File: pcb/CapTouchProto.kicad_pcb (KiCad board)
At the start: 2 copper layers, 12 parts, among them J1 62684-50110, U1 1965-ESP32-WROOM-32E(8MB)CT-ND

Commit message: A little layout.
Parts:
- added C4: 0.1μF, Capacitor_SMD:C_0603_1608Metric, F.Cu at (161.7, 155.1)
- added C5: 0.1μF, Capacitor_SMD:C_0603_1608Metric, F.Cu at (141.8, 126.2)
- added C6: 22μF, Capacitor_SMD:C_0603_1608Metric, F.Cu at (136.7, 123.8)
- added C7: 0.1μF, Capacitor_SMD:C_0603_1608Metric, F.Cu at (136.7, 125.5)
- added C8: 22μF, Capacitor_SMD:C_0603_1608Metric, F.Cu at (129.5, 134.0)
- added C9: 22μF, Capacitor_SMD:C_0603_1608Metric, F.Cu at (136.7, 127.9)
- added D1: BAT760-7, Diode_SMD:D_SOD-323, F.Cu at (108.8, 129.3)
- added D2: SP0503BAHT, Package_TO_SOT_SMD:SOT-143, F.Cu at (173.5, 135.8)
- added D3: LED (red), LED_SMD:LED_0603_1608Metric, F.Cu at (136.5, 138.7)
- added Q1: S8050, Package_TO_SOT_THT:TO-92_Inline, F.Cu at (163.7, 115.1)
- added Q2: S8050, Package_TO_SOT_THT:TO-92_Inline, F.Cu at (164.4, 111.2)
- added R10: 10K, Resistor_SMD:R_0603_1608Metric, F.Cu at (168.0, 113.1)
- added R11: 10KΩ, Resistor_SMD:R_0603_1608Metric, F.Cu at (140.0, 126.2)
- added R12: 2K (5%), Resistor_SMD:R_0603_1608Metric, F.Cu at (133.4, 138.7)
- added R13: 2K2Ω, Resistor_SMD:R_0603_1608Metric, F.Cu at (136.6, 98.1)
- added R14: 2K2Ω, Resistor_SMD:R_0603_1608Metric, F.Cu at (136.6, 96.3)
- added R15: 68Ω, Resistor_SMD:R_0603_1608Metric, F.Cu at (159.6, 92.1)
- added R16: 68Ω, Resistor_SMD:R_0603_1608Metric, F.Cu at (159.6, 93.9)
- added R17: 68Ω, Resistor_SMD:R_0603_1608Metric, F.Cu at (159.6, 95.8)
- added R18: 68Ω, Resistor_SMD:R_0603_1608Metric, F.Cu at (159.6, 97.6)
- added R8: 10KΩ, Resistor_SMD:R_0603_1608Metric, F.Cu at (132.0, 157.0)
- added R9: 10K, Resistor_SMD:R_0603_1608Metric, F.Cu at (160.2, 113.1)
- added SW1: SW_Push, Button_Switch_THT:SW_PUSH_6mm_H4.3mm, F.Cu at (148.1, 96.3)
- added SW2: SW_Push, Button_Switch_THT:SW_PUSH_6mm_H4.3mm, F.Cu at (159.3, 151.3)
- added U2: 1965-ESP32-WROOM-32E(8MB)CT-ND, RF_Module:ESP32-WROOM-32, F.Cu at (144.5, 113.0)
- added U3: AMS1117-3.3, Package_TO_SOT_SMD:SOT-223-3_TabPin2, F.Cu at (136.6, 132.7)
- C1: value 22μF -> 4.7μF/6.3V; footprint Capacitor_SMD:C_0201_0603Metric -> Capacitor_SMD:C_0603_1608Metric
- C2: value 0.1μF -> 0.1μF/50V; footprint Capacitor_SMD:C_0201_0603Metric -> Capacitor_SMD:C_0603_1608Metric
- C3: value TBD -> 0.1μF; footprint Capacitor_SMD:C_0201_0603Metric -> Capacitor_SMD:C_0603_1608Metric
- R1: value 2K2Ω -> 22.1KΩ; footprint Resistor_SMD:R_0201_0603Metric -> Resistor_SMD:R_0603_1608Metric
- R2: value 2K2Ω -> 47.5KΩ; footprint Resistor_SMD:R_0201_0603Metric -> Resistor_SMD:R_0603_1608Metric
- R3, R5: value 68Ω -> 5K1Ω; footprint Resistor_SMD:R_0201_0603Metric -> Resistor_SMD:R_0603_1608Metric
- R4: value 68Ω -> 2KΩ; footprint Resistor_SMD:R_0201_0603Metric -> Resistor_SMD:R_0603_1608Metric
- R6: value 68Ω -> 0Ω; footprint Resistor_SMD:R_0201_0603Metric -> Resistor_SMD:R_0603_1608Metric
- R7: value TBDΩ -> 0Ω; footprint Resistor_SMD:R_0201_0603Metric -> Resistor_SMD:R_0603_1608Metric
- U1: value 1965-ESP32-WROOM-32E(8MB)CT-ND -> CP2102N-A01-GQFN28; footprint RF_Module:ESP32-WROOM-32 -> Package_DFN_QFN:QFN-28-1EP_5x5mm_P0.5mm_EP3.35x3.35mm
- moved C2 84.3 mm to (115.7, 146.4), turned to 270 degrees
- moved R3 83.0 mm to (108.8, 138.4), turned to 180 degrees
- moved R2 74.6 mm to (135.3, 148.2)
- moved R1 70.1 mm to (145.9, 144.8)
- moved R4 68.3 mm to (136.7, 143.7), turned to 180 degrees
- moved U1 52.7 mm to (122.3, 144.1)
- moved R7 51.9 mm to (141.5, 101.3), turned to 90 degrees
- moved C1 40.1 mm to (117.5, 146.4), turned to 270 degrees
- moved R5 37.6 mm to (108.6, 134.1), turned to 180 degrees
- moved C3 35.6 mm to (150.2, 86.6)
- moved R6 31.1 mm to (139.8, 101.3), turned to 90 degrees
- moved J2 9.79 mm to (174.1, 85.9), turned to 90 degrees
- renumbered J1 to J2
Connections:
- C1 pad 1: +3V3 -> VBUS
- C2 pad 1: +3V3 -> VBUS
- C3 pad 1: Net-(C3-Pad1) -> GND
- C3 pad 2: GND -> IO0
- J2 pad 10: Net-(J1-Pad10) -> Net-(J2-Pad10)
- J2 pad 2: Net-(J1-Pad2) -> Net-(J2-Pad2)
- J2 pad 3: Net-(J1-Pad3) -> Net-(J2-Pad3)
- J2 pad 33: Net-(J1-Pad33) -> Net-(J2-Pad33)
- J2 pad 34: Net-(J1-Pad34) -> Net-(J2-Pad34)
- J2 pad 36: Net-(J1-Pad36) -> Net-(J2-Pad36)
- J2 pad 37: Net-(J1-Pad37) -> Net-(J2-Pad37)
- J2 pad 38: Net-(J1-Pad38) -> Net-(J2-Pad38)
- J2 pad 4: Net-(J1-Pad4) -> Net-(J2-Pad4)
- J2 pad 44: Net-(J1-Pad44) -> Net-(J2-Pad44)
- J2 pad 45: Net-(J1-Pad45) -> Net-(J2-Pad45)
- J2 pad 46: Net-(J1-Pad46) -> Net-(J2-Pad46)
- J2 pad 47: Net-(J1-Pad10) -> Net-(J2-Pad10)
- J2 pad 5: Net-(J1-Pad5) -> Net-(J2-Pad5)
- R1 pad 1: +3V3 -> VBUS
- R1 pad 2: Net-(J1-Pad44) -> Net-(R1-Pad2)
- R2 pad 1: +3V3 -> Net-(R1-Pad2)
- R2 pad 2: Net-(J1-Pad45) -> GND
- R3 pad 1: Net-(J1-Pad2) -> Net-(J1-PadA5)
- R3 pad 2: +5V -> GND
- R4 pad 1: Net-(J1-Pad3) -> +3V3
- R4 pad 2: +5V -> Net-(R4-Pad2)
- R5 pad 1: Net-(J1-Pad4) -> Net-(J1-PadA5)
- R5 pad 2: +5V -> Net-(R5-Pad2)
- R6 pad 1: Net-(J1-Pad5) -> TXD
- R6 pad 2: +5V -> Net-(R6-Pad2)
- R7 pad 1: +3V3 -> RXD
- R7 pad 2: Net-(C3-Pad1) -> Net-(R7-Pad2)
- U1 pad 1: GND -> Net-(U1-Pad1)
- U1 pad 10: Net-(J1-Pad46) -> Net-(U1-Pad10)
- U1 pad 11: Net-(J1-Pad36) -> Net-(R8-Pad1)
- U1 pad 12: Net-(J1-Pad10) -> Net-(U1-Pad12)
- U1 pad 15: GND -> Net-(U1-Pad15)
- U1 pad 2: +3V3 -> Net-(U1-Pad2)
- U1 pad 24: Net-(U1-Pad24) -> RTS
- U1 pad 25: Net-(U1-Pad25) -> Net-(R6-Pad2)
- U1 pad 26: Net-(U1-Pad26) -> Net-(R7-Pad2)
- U1 pad 28: Net-(U1-Pad28) -> DTR
- U1 pad 29: Net-(J1-Pad38) -> GND
- U1 pad 3: Net-(C3-Pad1) -> GND
- U1 pad 4: Net-(U1-Pad4) -> D+
- U1 pad 5: Net-(U1-Pad5) -> D-
- U1 pad 6: Net-(U1-Pad6) -> VBUS
- U1 pad 7: Net-(U1-Pad7) -> VBUS
- U1 pad 8: Net-(U1-Pad8) -> Net-(R1-Pad2)
- U1 pad 9: Net-(U1-Pad9) -> Net-(R4-Pad2)
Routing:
- net GND: track 0.00 -> 27.9 mm
- net +3V3: track 0.00 -> 15.1 mm
- net Net-(J2-Pad45): track 0.00 -> 11.6 mm
- net VBUS: track 0.00 -> 11.2 mm
- net Net-(J2-Pad44): track 0.00 -> 6.93 mm
- net EN: track 0.00 -> 6.23 mm
- net Net-(D3-Pad2): track 0.00 -> 3.13 mm
- net TXD: track 0.00 -> 2.42 mm
- net RXD: track 0.00 -> 2.38 mm

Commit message: more layout.
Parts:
- added J1: USB_C_Receptacle, Connector_USB:USB_C_Receptacle_Amphenol_12401548E4-2A, F.Cu at (179.3, 147.1)
- moved R3 73.4 mm to (182.2, 136.8), turned to 270 degrees
- moved R5 69.8 mm to (178.4, 136.9), turned to 90 degrees
- moved C1 64.3 mm to (176.8, 121.6)
- moved C2 64.3 mm to (175.0, 121.6)
- moved U1 64.0 mm to (180.8, 118.2)
- moved D1 61.7 mm to (169.9, 137.2), turned to 270 degrees
- moved R8 59.2 mm to (181.7, 124.8), turned to 270 degrees
- moved R4 46.7 mm to (179.3, 124.8), turned to 90 degrees
- moved R2 41.7 mm to (169.0, 123.7), turned to 270 degrees
- moved R1 33.3 mm to (171.6, 123.7), turned to 270 degrees
- moved C4 24.9 mm to (158.1, 130.5), turned to 90 degrees
- moved SW2 19.1 mm to (154.2, 132.8), turned to 180 degrees
- moved C3 18.0 mm to (133.5, 80.1)
- moved SW1 18.0 mm to (131.3, 89.9)
- moved J2 9.78 mm to (183.9, 85.9)
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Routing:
- net Net-(J2-Pad44): track 6.93 -> 102.2 mm
- net +3V3: track 15.1 -> 94.6 mm, vias 0 -> 1
- net Net-(J2-Pad10): track 0.00 -> 75.1 mm, vias 0 -> 6
- net VCC: track 0.00 -> 72.7 mm, vias 0 -> 3
- net Net-(J2-Pad46): track 0.00 -> 72.3 mm, vias 0 -> 4
- net Net-(J2-Pad45): track 11.6 -> 77.9 mm, vias 0 -> 2
- net Net-(J2-Pad36): track 0.00 -> 64.1 mm, vias 0 -> 4
- net Net-(J2-Pad34): track 0.00 -> 63.4 mm, vias 0 -> 4
- net Net-(J2-Pad38): track 0.00 -> 57.8 mm
- net Net-(J2-Pad37): track 0.00 -> 55.6 mm
- net Net-(J2-Pad33): track 0.00 -> 52.0 mm
- net IO0: track 0.00 -> 52.0 mm, vias 0 -> 2
- net Net-(R6-Pad2): track 0.00 -> 51.3 mm, vias 0 -> 2
- net Net-(R7-Pad2): track 0.00 -> 47.4 mm, vias 0 -> 2
- net GND: track 27.9 -> 68.5 mm, vias 0 -> 37
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- added copper zone on B.Cu, net GND
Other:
- board outline added: 75.8 x 75.5 mm

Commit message: Layout of usb-c power.
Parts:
- moved R5 21.5 mm to (157.9, 143.4)
- moved R2 13.3 mm to (181.4, 128.6), turned to 0 degrees
- moved J1 11.8 mm to (173.5, 136.8)
- moved D1 9.28 mm to (170.3, 128.0), turned to 0 degrees
- moved R1 8.64 mm to (179.7, 126.6), turned to 0 degrees
- moved D2 6.96 mm to (170.4, 125.0)
- moved R3 6.76 mm to (188.3, 139.6)
- moved R4 2.58 mm to (181.6, 123.6)
- moved R8 2.10 mm to (183.4, 123.6)
- moved C1 1.94 mm to (178.1, 123.1)
- moved C2 1.94 mm to (176.3, 123.1)
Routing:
- net Net-(D1-Pad2): track 0.00 -> 36.2 mm
- net D-: track 0.00 -> 23.1 mm, vias 0 -> 2
- net D+: track 0.00 -> 18.7 mm
- net GND: track 68.5 -> 80.2 mm, vias 37 -> 42
- net Net-(R1-Pad2): track 0.00 -> 8.46 mm
- net VBUS: track 15.9 -> 23.6 mm

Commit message: Getting closer.
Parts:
- moved R5 33.0 mm to (189.5, 133.9)
- moved R3 5.73 mm to (182.6, 139.3), turned to 90 degrees
- moved R2 2.57 mm to (183.0, 126.6)
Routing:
- net VBUS: track 23.6 -> 106.8 mm
- net +3V3: track 94.6 -> 152.7 mm, vias 1 -> 3
- net Net-(J1-PadA5): track 0.00 -> 36.0 mm, vias 0 -> 4
- net Net-(J1-PadS1): track 0.00 -> 22.2 mm
- net D+: track 18.7 -> 28.8 mm, vias 0 -> 1
- net D-: track 23.1 -> 31.7 mm, vias 2 -> 3
- net GND: track 80.2 -> 85.5 mm, vias 42 -> 44
- net Net-(D1-Pad2): track 36.2 -> 37.0 mm
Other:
- board size 75.8 x 75.5 mm -> 73.5 x 64 mm

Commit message: Transistors to SOT-23.
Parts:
- Q1, Q2: value S8050 -> SS8050-G; footprint Package_TO_SOT_THT:TO-92_Inline -> Package_TO_SOT_SMD:SOT-23
- moved Q2 0.70 mm to (160.1, 109.3)
- moved R10 0.63 mm to (161.0, 113.9)
- moved R9 0.25 mm to (159.1, 113.9)
- renumbered SW1 to BOOT1, SW2 to EN1
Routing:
- net Net-(Q2-Pad2): track 6.60 -> 2.81 mm
- net Net-(Q1-Pad2): track 6.32 -> 2.62 mm
- net RTS: track 32.1 -> 29.1 mm, vias 1 -> 2
- net EN: track 34.1 -> 35.9 mm
- net IO0: track 52.0 -> 53.3 mm

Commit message: power routed.
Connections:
- J2 pad 40: VCC -> +3V3
- J2 pad 41: VCC -> +3V3
- J2 pad 42: VCC -> +3V3
- J2 pad 7: VCC -> +3V3
- J2 pad 8: VCC -> +3V3
- J2 pad 9: VCC -> +3V3
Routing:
- net VCC: track 72.7 -> 0.00 mm, vias 3 -> 0
- net +3V3: track 152.7 -> 224.2 mm, vias 3 -> 6

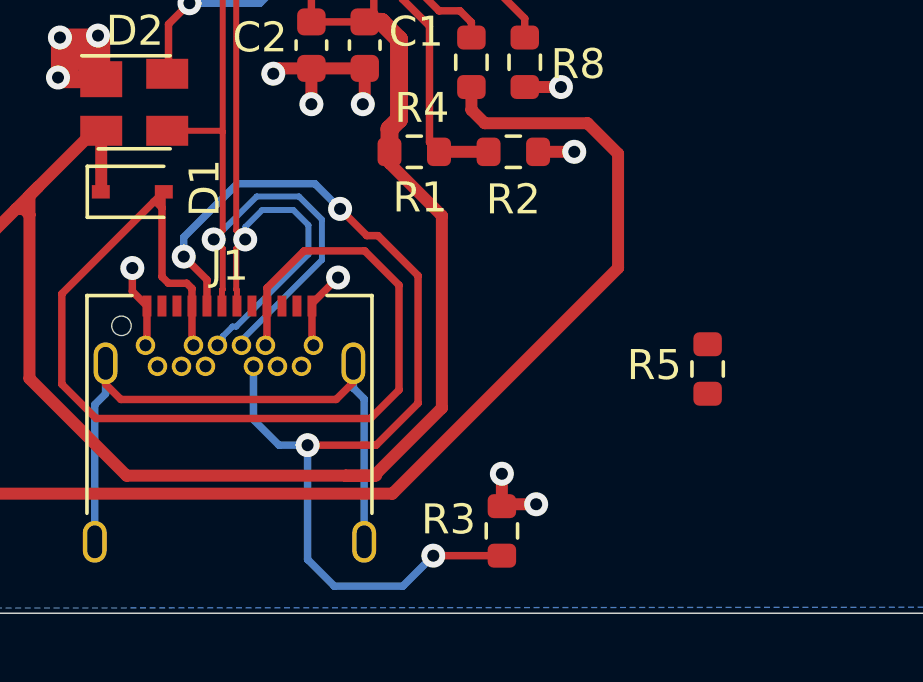
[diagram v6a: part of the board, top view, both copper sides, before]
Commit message: USB-C 5.1K resistor layout.
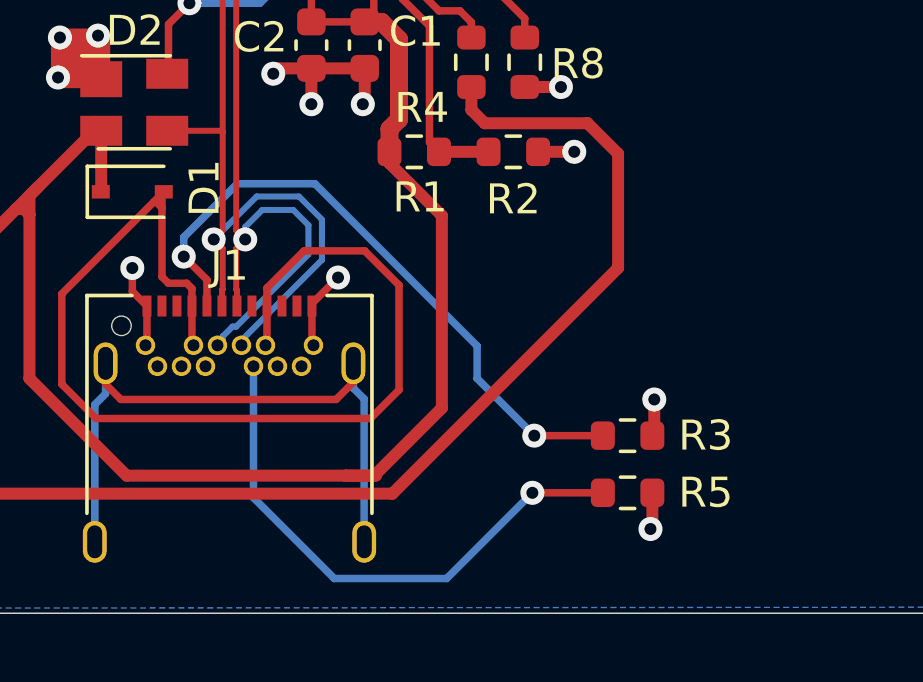
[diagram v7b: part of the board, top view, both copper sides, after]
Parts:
- moved R3 5.26 mm to (186.8, 136.1), turned to 0 degrees
- moved R5 4.91 mm to (186.8, 138.0), turned to 0 degrees
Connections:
- J1 pad B5: Net-(J1-PadA5) -> Net-(J1-PadB5)
- R5 pad 1: Net-(J1-PadA5) -> Net-(J1-PadB5)
- R5 pad 2: Net-(R5-Pad2) -> GND
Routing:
- net Net-(J1-PadB5): track 0.00 -> 18.3 mm, vias 0 -> 1
- net Net-(J1-PadA5): track 36.0 -> 21.4 mm, vias 4 -> 2

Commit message: Layout done.
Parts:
- moved C8 1.59 mm to (131.1, 134.0)
- renumbered BOOT1 to BOOT, EN1 to EN
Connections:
- J2 pad 1: Net-(J2-Pad1) -> VBUS
- R15 pad 2: +5V -> VBUS
- R16 pad 2: +5V -> VBUS
- R17 pad 2: +5V -> VBUS
- R18 pad 2: +5V -> VBUS
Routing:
- net VBUS: track 106.8 -> 222.2 mm, vias 0 -> 2
- net GND: track 85.8 -> 76.3 mm
- net +3V3: track 224.2 -> 230.5 mm
- net +5V: track 5.52 -> 0.00 mm
